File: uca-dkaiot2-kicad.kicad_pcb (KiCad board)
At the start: 4 copper layers, 195.9 x 119.2 mm, 176 parts, among them J1 Conn_01x04, J10 Conn_Coaxial, J11 Conn_01x02, J12 Conn_01x02, J13 Conn_ARM_SWD_TagConnect_TC203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, J2J14 Conn_02x06_Odd_Even, J3 Conn_01x02, J4 Conn_01x02, J5 Conn_01x02, J6 Conn_Coaxial, J7 Conn_01x05, J8 USB_B_Micro, J9 Conn_ARM_SWD_TagConnect_TC203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, U1 NCV8170AXV300T2G, U10 NCV8170AXV300T2G, U11 DRV5023AJxLPG, U12 R5478N101CD, U13 FDV301N, U14 FDV301N, U15 R5478N101CD, U16 FDV301N, U17 FDV301N, U18 LTR-303ALS-01, U19 ICM-20948, U2 Quectel_L96, U20 KXTJ3-1057, U21 HP203B, U22 SPH0645LM4H, U24 KX023-1025, U26 NCV8170BXV180T2G, U28 BSS138L, U29 SGP30, U3 Conn_01x04, U30 BSS138L, U31 BSS138L, U32 Micro_SD_Card_Det1, U33 NCV8170AXV300T2G, U4 STM32U595RITx, U5 E22-900M22S, U6 LSM303AH, U7 BME280, U8 ATECC608A-SSHDA, U9 MCP73831-2-OT, X1 SMD3225-4, X2 SMD2012-2

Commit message: pcb: 2-layer stackup
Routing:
- net GND: track 4282.3 -> 2917.3 mm
- removed copper zone on In2.Cu, net GND
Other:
- copper layers 4 -> 2

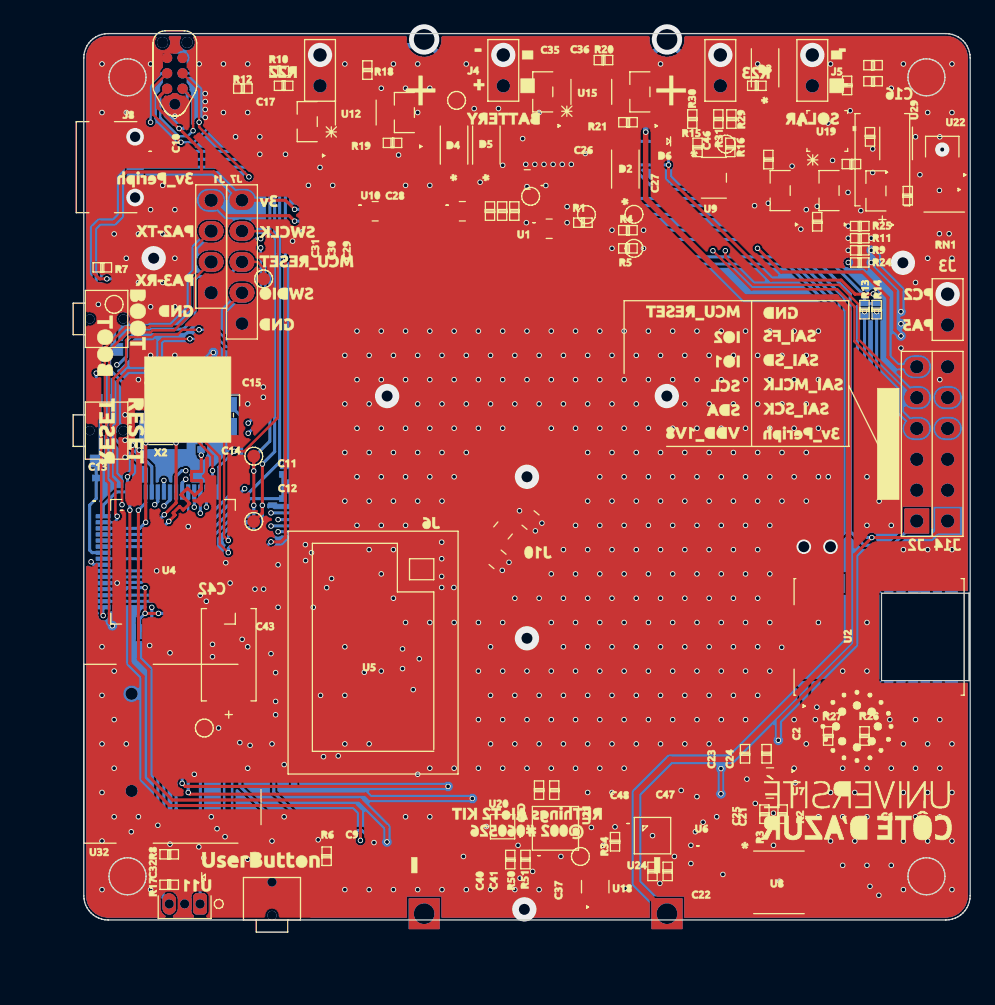
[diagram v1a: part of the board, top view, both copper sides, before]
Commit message: pcb: remove original AIoT2 design
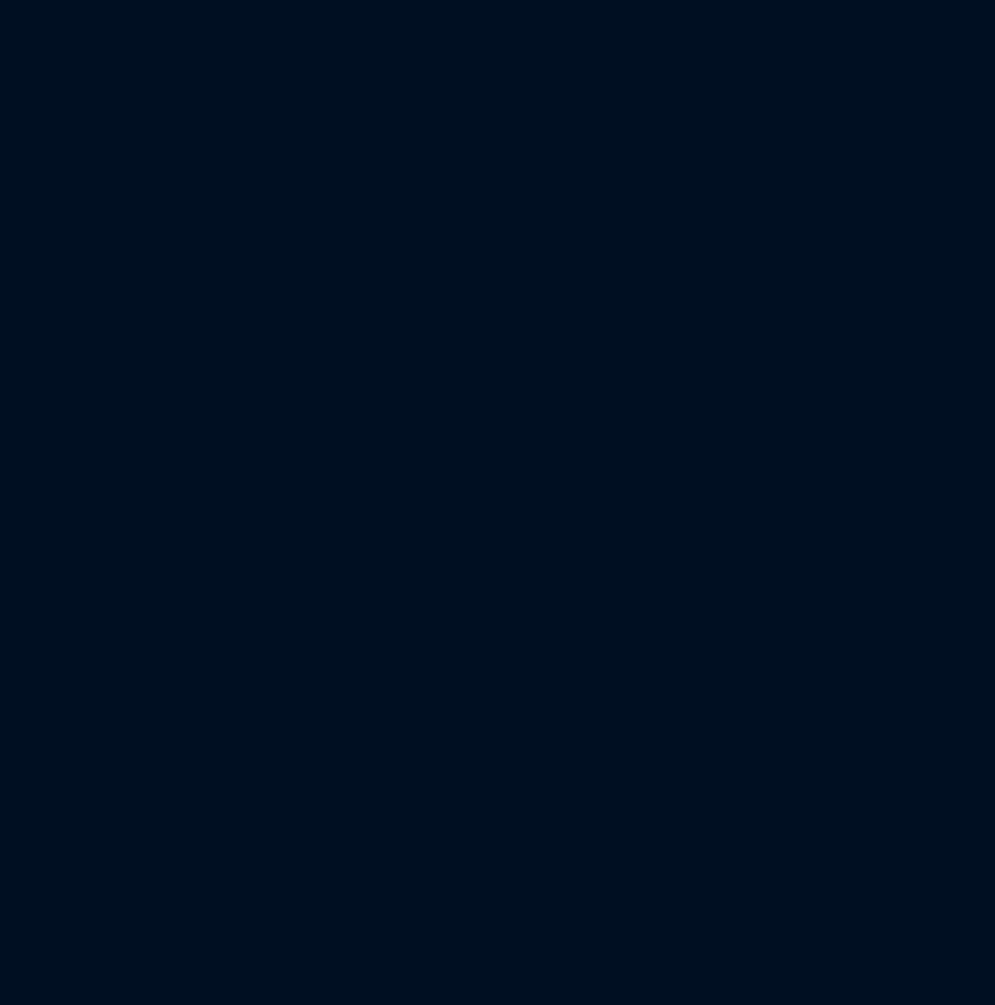
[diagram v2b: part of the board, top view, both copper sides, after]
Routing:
- net GND: track 2917.3 -> 0.00 mm, vias 708 -> 0
- net (no net): track 89.1 -> 0.00 mm
- net USB+: track 52.9 -> 0.00 mm
- net TIMEPULSE: track 37.9 -> 0.00 mm
- net INT_ACC_2: track 24.1 -> 0.00 mm
- net V_PERIPH_ON_OFF: track 22.7 -> 0.00 mm
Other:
- board size 195.9 x 119.2 mm -> 73 x 73 mm

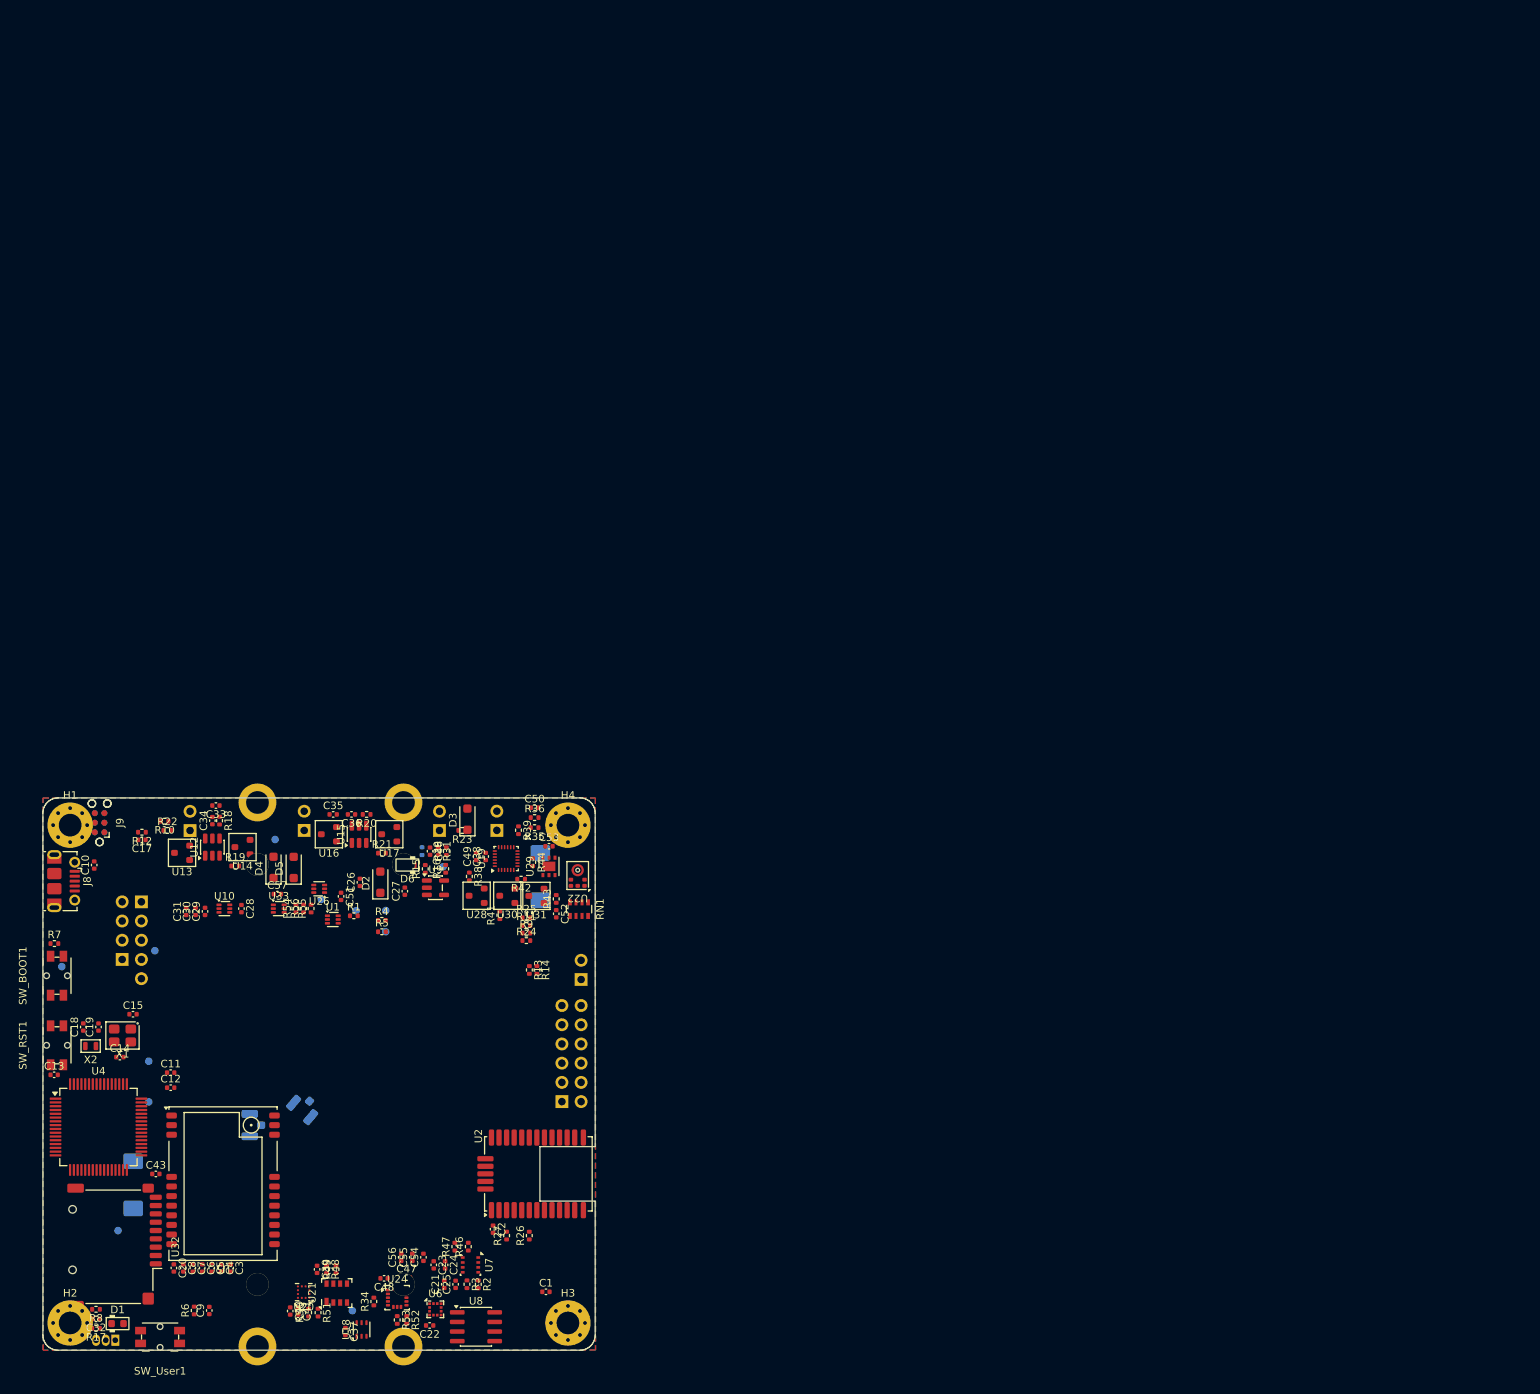
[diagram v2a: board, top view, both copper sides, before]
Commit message: pcb: start 2-layer routing
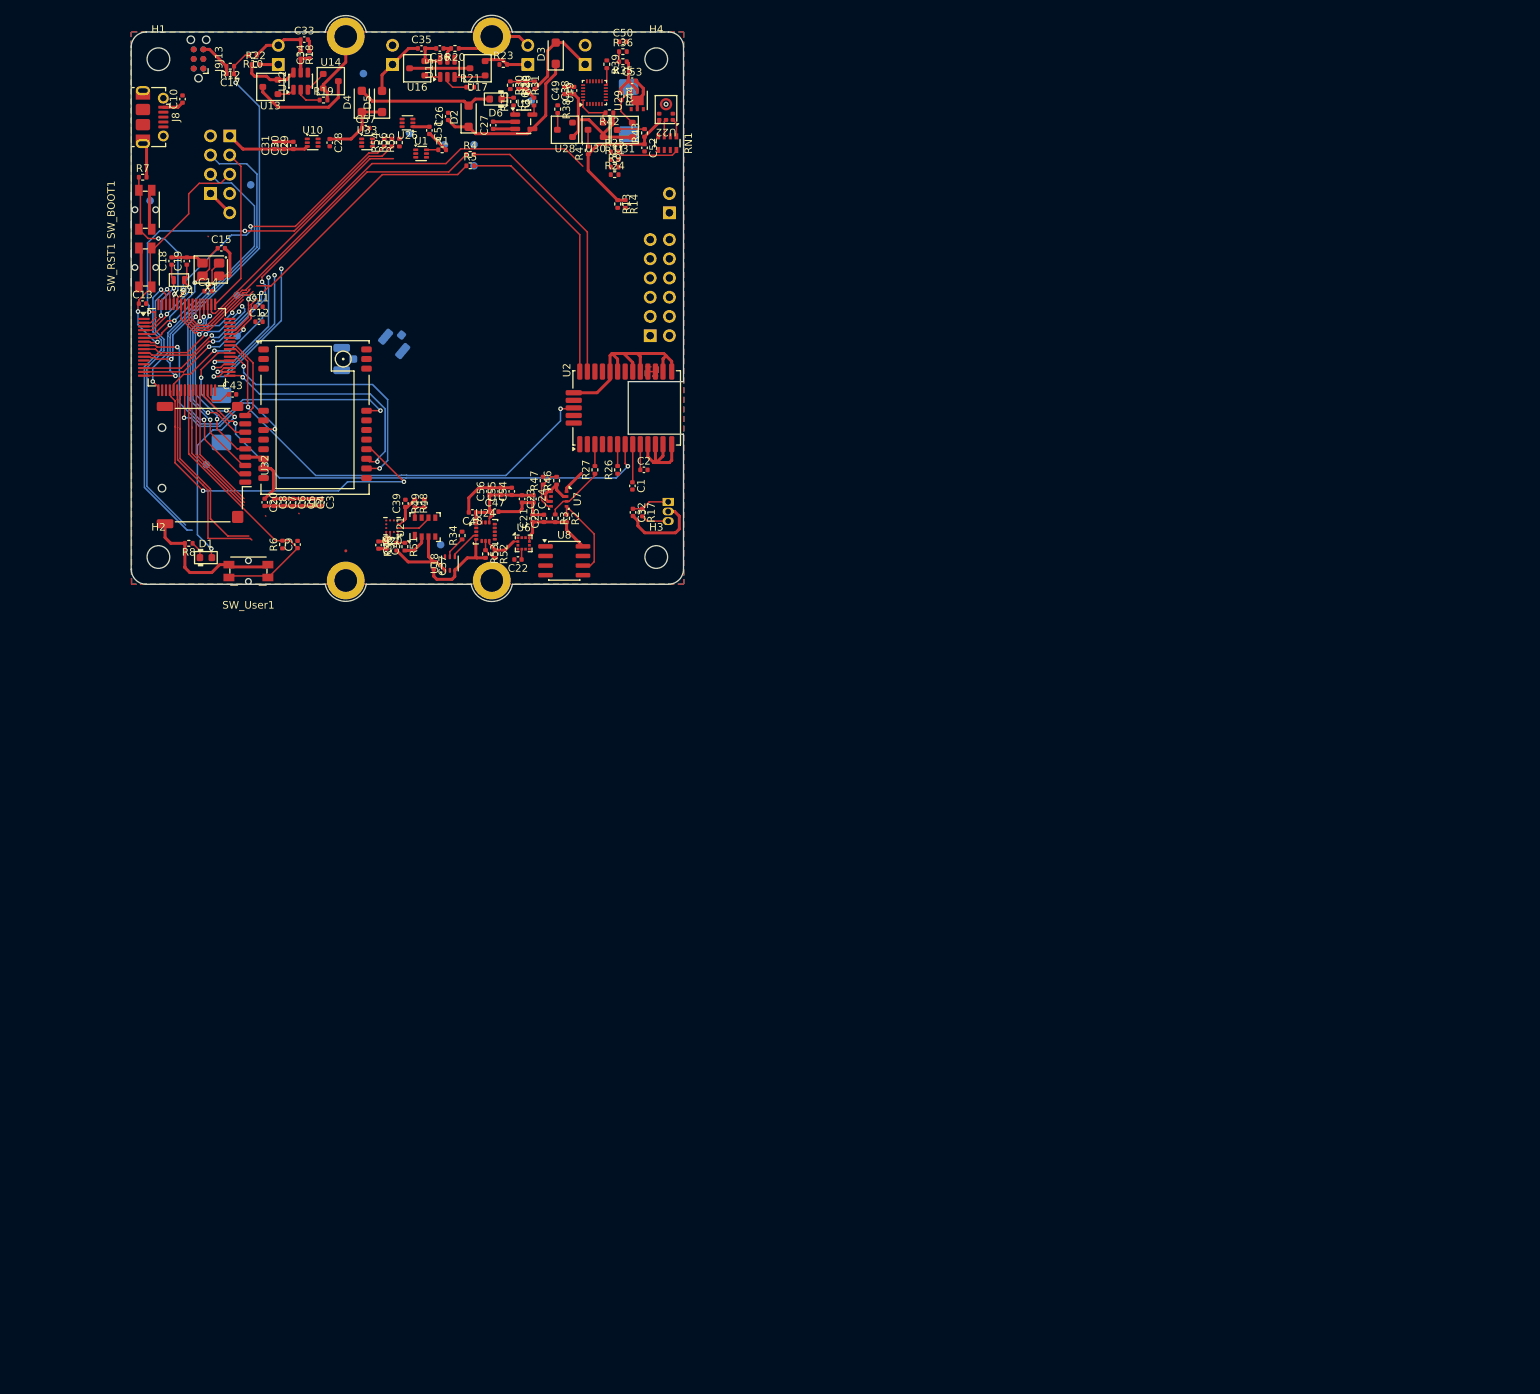
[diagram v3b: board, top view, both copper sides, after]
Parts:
- removed J13: Conn_ARM_SWD_TagConnect_TC2030-NL, Connector:Tag-Connect_TC2030-IDC-NL_2x03_P1.27mm_Vertical
- H1, H2, H3, H4: value MountingHole_Pad -> MountingHole; footprint MountingHole:MountingHole_3mm_Pad_Via -> MountingHole:MountingHole_3mm
- J9J13: renamed from J9; footprint Connector:Tag-Connect_TC2030-IDC-NL_2x03_P1.27mm_Vertical -> footprints:Tag-Connect_TC2030-IDC-NL_2x03_P1.27mm_Vertical_TopBottom
- R30: moved to F.Cu
- moved U11 132.7 mm to (96.0, 84.1), turned to -90 degrees
- moved R17 129.8 mm to (92.6, 85.5), turned to -90 degrees
- moved C32 128.1 mm to (91.3, 85.5), turned to -90 degrees
- moved C1 107.1 mm to (91.2, 82.0), turned to -90 degrees
- moved U32 104.0 mm to (34.6, 79.2)
- moved U4 103.7 mm to (32.4, 63.7)
- moved C43 103.5 mm to (38.4, 69.9)
- moved SW_RST1 103.5 mm to (26.9, 53.1)
- moved C13 102.6 mm to (26.5, 57.9)
- moved C2 102.3 mm to (92.8, 79.9), turned to 0 degrees
- moved R15 102.1 mm to (75.5, 31.2)
- moved R38 102.1 mm to (81.4, 32.2)
- moved R16 102.1 mm to (78.2, 31.2)
- moved C34 102.0 mm to (48.5, 25.0)
- moved J_RST1 102.0 mm to (40.8, 42.2)
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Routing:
- net GND: track 0.00 -> 177.5 mm
- net V_PERIPH_3V: track 0.00 -> 85.1 mm
- net GPS_INT: track 0.00 -> 65.9 mm, vias 0 -> 2
- net Net-(U4-PB3): track 0.00 -> 64.8 mm
- net TIMEPULSE: track 0.00 -> 60.6 mm, vias 0 -> 2
- net GPS_TXD: track 0.00 -> 57.0 mm, vias 0 -> 2
- net I2C1_SCL: track 0.00 -> 56.9 mm, vias 0 -> 1
- net GPS_RXD: track 0.00 -> 55.9 mm, vias 0 -> 2
- net I2C1_SDA: track 0.00 -> 53.8 mm, vias 0 -> 1
- net VBAT_MEASURE: track 0.00 -> 51.3 mm, vias 0 -> 2
- net SD_ON_OFF: track 0.00 -> 50.3 mm, vias 0 -> 2
- net NRST_E22: track 0.00 -> 48.9 mm, vias 0 -> 2
- net PA2_TX: track 0.00 -> 43.5 mm, vias 0 -> 1
- net NSS_E22: track 0.00 -> 43.5 mm, vias 0 -> 2
- net UserButton: track 0.00 -> 38.8 mm
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- added copper zone on B.Cu, net Net-(U2-RF_IN)
- added copper zone on F.Cu, net Net-(U2-RF_IN)
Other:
- board size 73 x 73 mm -> 73 x 77.5 mm

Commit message: pcb: continue routing
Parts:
- moved R4 2.88 mm to (72.5, 39.2)
- moved R5 2.88 mm to (72.5, 40.7)
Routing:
- net HALL_On_Off: track 7.43 -> 90.0 mm
- net I2C3_SDA: track 18.5 -> 101.0 mm, vias 2 -> 3
- net I2C1_SCL: track 56.9 -> 137.2 mm, vias 1 -> 5
- net I2C1_SDA: track 53.8 -> 134.0 mm, vias 1 -> 7
- net EXT_MIC_IO_1: track 0.00 -> 76.0 mm, vias 0 -> 2
- net I2C3_SCL: track 21.2 -> 94.7 mm, vias 2 -> 4
- net PA5_DAC_ADC: track 16.7 -> 87.4 mm, vias 2 -> 1
- net MCU_RESET: track 32.4 -> 99.3 mm, vias 2 -> 6
- net Net-(U1-OUT): track 3.39 -> 69.1 mm, vias 0 -> 2
- net HALL_OUT: track 28.5 -> 89.0 mm, vias 0 -> 1
- net V_BCKP_On_Off: track 32.3 -> 91.7 mm, vias 0 -> 2
- net Net-(U4-PB5): track 13.7 -> 72.2 mm, vias 0 -> 2
- net Net-(U4-PB6): track 13.1 -> 71.1 mm
- net Net-(U4-PB4): track 12.7 -> 70.0 mm, vias 0 -> 2
- net V_PERIPH_3V: track 85.1 -> 139.5 mm, vias 0 -> 5
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
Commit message: pcb: continue routing
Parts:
- moved R4 0.85 mm to (72.5, 40.0)
- moved R5 0.85 mm to (72.5, 41.5)
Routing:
- net GND: track 203.3 -> 1055.9 mm, vias 1 -> 131
- net V_PERIPH_3V: track 139.5 -> 322.6 mm, vias 5 -> 12
- net +BATT1_IN: track 29.6 -> 177.7 mm, vias 0 -> 3
- net +3V: track 66.9 -> 208.9 mm, vias 5 -> 13
- net -BATT2_IN: track 5.99 -> 128.9 mm, vias 0 -> 2
- net +5V: track 20.9 -> 116.4 mm, vias 0 -> 5
- net VDD_1V8: track 25.7 -> 113.0 mm, vias 0 -> 4
- net PC2_ADC: track 16.9 -> 102.1 mm, vias 2 -> 5
- net I2C1_SCL: track 137.2 -> 201.8 mm, vias 5 -> 7
- net I2C1_SDA: track 134.0 -> 193.4 mm, vias 7 -> 9
- net ICM_INT: track 17.4 -> 76.6 mm, vias 2 -> 4
- net GPS_On_Off: track 20.7 -> 54.5 mm, vias 2 -> 4
- net MCU_RESET: track 99.3 -> 130.0 mm, vias 6 -> 9
- net SWDIO: track 24.9 -> 47.7 mm, vias 1 -> 4
- net E22_ANT: track 0.00 -> 13.6 mm, vias 0 -> 2
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- added copper zone on B.Cu, net (none)
- added copper zone on F.Cu, net (none)
